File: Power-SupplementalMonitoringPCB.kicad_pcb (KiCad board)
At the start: 2 copper layers, 67.5 x 62.5 mm, 66 parts, among them J1 SWD, J2 CAN_Out, J3 CAN_Out, J4 PowerConn, J5 SuppPowerConnector, SW1 Reset, U1 STM32F413RHTx, U10 Si87xx, U2 ADM3055E, U3 CDSOT23-T24CAN, U4 RI3-1205S, U5 NCP1117-3.3_SOT223, U6 REF34-Q1, U7 OPAx192-Q1, U8 OPA388-Q1, U9 OPA388-Q1, Y1 8M

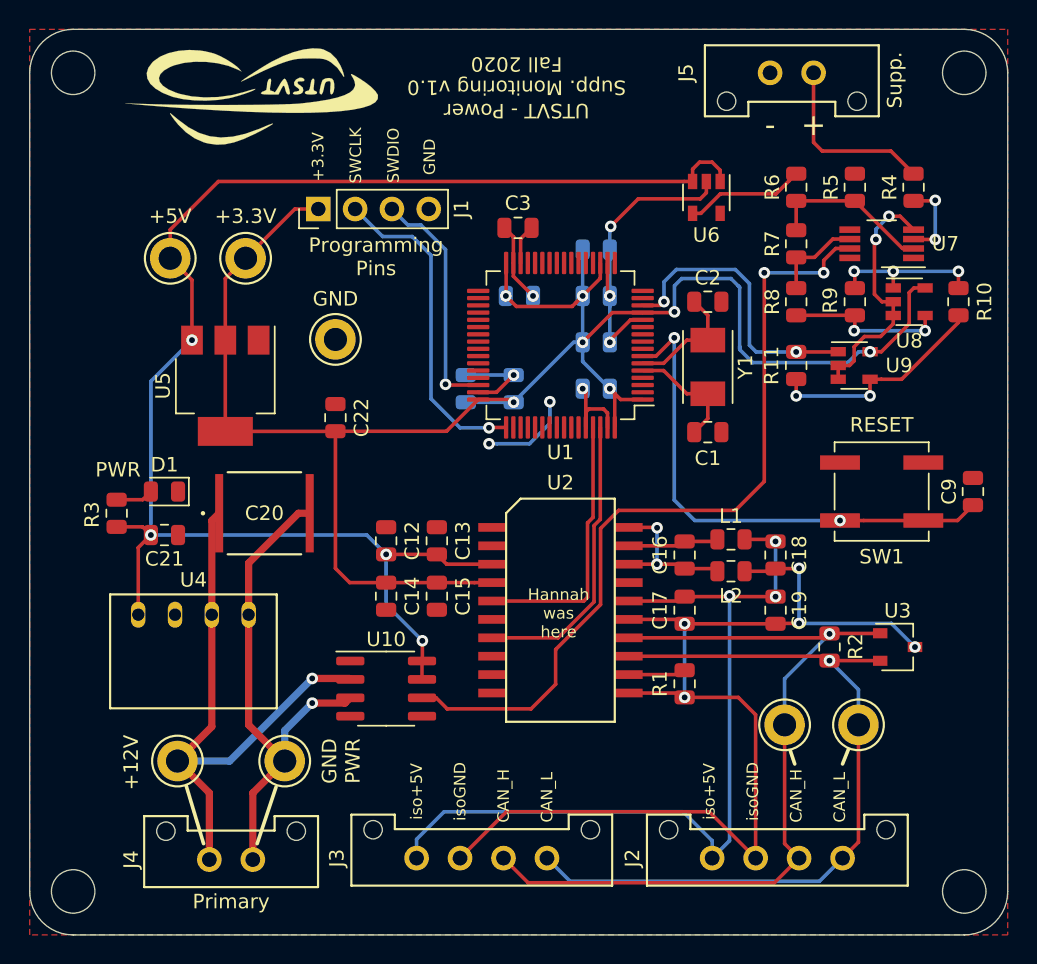
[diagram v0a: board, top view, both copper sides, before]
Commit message: Makes edits from critical design review
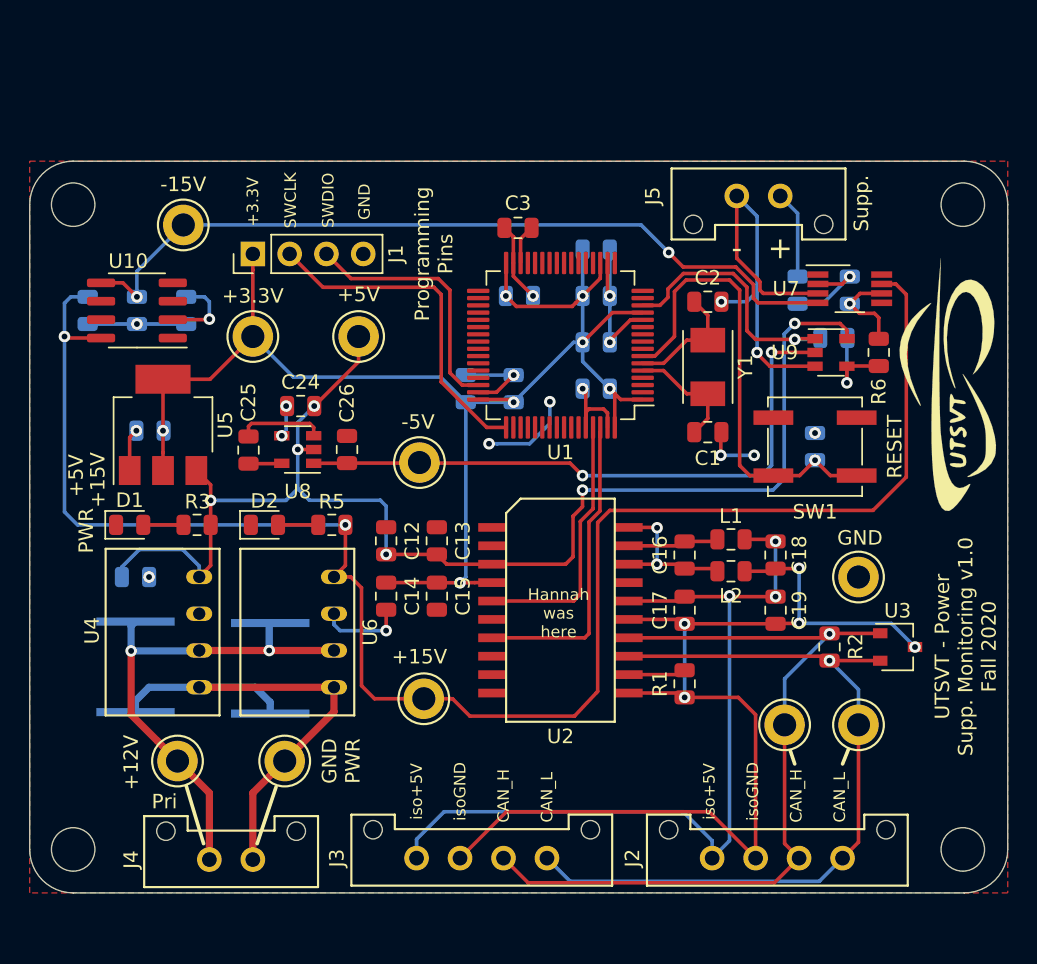
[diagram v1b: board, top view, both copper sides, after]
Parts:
- removed R10, R11, R9: 10k, Resistor_SMD:R_0805_2012Metric
- added C23: 10u, UTSVT_Passive:C_2220_5750Metric, B.Cu at (110.6, 98.5)
- added C24: 1u, Capacitor_SMD:C_0805_2012Metric, F.Cu at (112.7, 80.4)
- added C25: 1u, Capacitor_SMD:C_0805_2012Metric, F.Cu at (109.1, 83.4)
- added C26: 1u, Capacitor_SMD:C_0805_2012Metric, F.Cu at (115.9, 83.4)
- added C27: 2.2u, Capacitor_SMD:C_0805_2012Metric, B.Cu at (98.0, 73.8)
- added C28: 10u, Capacitor_SMD:C_0805_2012Metric, B.Cu at (104.8, 73.8)
- added C29: 10u, Capacitor_SMD:C_0805_2012Metric, B.Cu at (101.4, 73.8)
- added D2: PowerOn, LED_SMD:LED_0805_2012Metric, F.Cu at (110.2, 88.6)
- added TP10: -15V_TP, TestPoint:TestPoint_Keystone_5005-5009_Compact, F.Cu at (104.6, 67.9)
- added TP8: +15V_TP, TestPoint:TestPoint_Keystone_5005-5009_Compact, F.Cu at (121.2, 100.6)
- added TP9: -5V_TP, TestPoint:TestPoint_Keystone_5005-5009_Compact, F.Cu at (120.9, 84.3)
- C20, C21, C22, C9: moved to B.Cu
- R4: value 20k -> 10k; moved to B.Cu
- R5: value 20k -> 6.2k
- R7: value 20k -> 2.2k; moved to B.Cu
- R8: value 27k -> 10k; moved to B.Cu
- U10: value Si87xx -> TC7662Bx0A
- U6: value REF34-Q1 -> RI3-1215S; footprint Package_TO_SOT_SMD:SOT-23-5 -> UTSVT_ICs:RI3_DC_Converter
- U8: value OPA388-Q1 -> TPS6040x-Q1
- moved LOGO2 52.0 mm to (157.5, 79.2), turned to 90 degrees
- moved U8 43.4 mm to (112.5, 83.4), turned to 180 degrees
- moved R5 43.0 mm to (114.8, 88.6), turned to 180 degrees
- moved TP6 39.7 mm to (151.2, 92.2)
- moved U6 39.5 mm to (115.0, 96.0), turned to 90 degrees
- moved U10 31.3 mm to (101.4, 73.8), turned to 180 degrees
- moved TP5 14.1 mm to (116.7, 75.6)
- moved C20 13.8 mm to (101.3, 98.4), turned to 270 degrees
- moved C22 12.8 mm to (102.3, 82.1), turned to 180 degrees
- moved R6 12.7 mm to (152.6, 76.7)
- moved C9 11.3 mm to (148.2, 83.2)
- moved R4 10.7 mm to (147.0, 72.4)
- moved H2 9.10 mm to (158.4, 66.5)
- moved H1 9.10 mm to (97.0, 66.5)
- moved J5 8.81 mm to (145.8, 65.9)
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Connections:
- R5 pad 1: Net-(R5-Pad1) -> +15V
- R5 pad 2: GND -> Net-(D2-Pad2)
- R6 pad 1: Net-(R5-Pad1) -> Net-(R6-Pad1)
- R7 pad 1: Net-(R7-Pad1) -> Net-(R6-Pad2)
- R7 pad 2: Net-(R5-Pad1) -> Net-(R4-Pad1)
- R8 pad 1: Net-(R8-Pad1) -> /SuppOut
- R8 pad 2: Net-(R7-Pad1) -> Net-(R6-Pad1)
- U10 pad 2: +12VA -> Net-(C28-Pad1)
- U10 pad 3: GNDPWR -> GND
- U10 pad 4: Net-(U10-Pad4) -> GND
- U10 pad 5: GND -> -15V
- U10 pad 6: +12V -> Net-(U10-Pad6)
- U10 pad 7: +5V -> Net-(U10-Pad7)
- U10 pad 8: +5V -> +15V
- U6 pad 1: +5V -> GNDPWR
- U6 pad 2: GND -> +12VA
- U6 pad 3: +5V -> GND
- U6 pad 4: Net-(R6-Pad2) -> +15V
- U7 pad 2: Net-(R5-Pad1) -> Net-(R4-Pad1)
- U7 pad 3: Net-(R4-Pad1) -> GND
- U7 pad 4: GND -> -15V
- U7 pad 6: Net-(R7-Pad1) -> Net-(R6-Pad2)
- U7 pad 7: +12V -> +15V
- U8 pad 1: Net-(R10-Pad2) -> -5V
- U8 pad 2: GND -> +5V
- U8 pad 3: GND -> Net-(C25-Pad1)
- U8 pad 4: Net-(R8-Pad1) -> GND
- U8 pad 5: +3V3 -> Net-(C25-Pad2)
- U9 pad 2: GND -> -5V
- U9 pad 4: Net-(R10-Pad1) -> Net-(R6-Pad1)
- U9 pad 5: +3V3 -> +5V
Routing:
- net +15V: track 0.00 -> 118.2 mm, vias 0 -> 2
- net +12V: track 56.4 -> 0.00 mm, vias 2 -> 0
- net -15V: track 0.00 -> 55.7 mm, vias 0 -> 2
- net -5V: track 0.00 -> 43.1 mm, vias 0 -> 2
- net +3V3: track 132.0 -> 100.6 mm
- net GND: track 63.7 -> 88.4 mm, vias 10 -> 18
- net Net-(R10-Pad1): track 15.6 -> 0.00 mm, vias 2 -> 0
- net +5V: track 106.8 -> 93.5 mm, vias 4 -> 6
- net Net-(R5-Pad1): track 11.5 -> 0.00 mm
- net Net-(R8-Pad1): track 11.1 -> 0.00 mm, vias 2 -> 0
- net Net-(R10-Pad2): track 10.7 -> 0.00 mm, vias 3 -> 0
- net Net-(J5-Pad1): track 12.6 -> 6.06 mm
- net Net-(R6-Pad1): track 0.00 -> 6.47 mm, vias 0 -> 1
- net Net-(R7-Pad1): track 6.35 -> 0.00 mm
- net Net-(C25-Pad1): track 0.00 -> 5.97 mm
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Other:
- board size 67.5 x 62.5 mm -> 67.5 x 50.5 mm
- board text added: "+15V"
- board text added: "-15V"
- board text added: "-5V"
- board text added: "Pri"
- board text removed: "Primary"

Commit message: Edits opamp circuitry to just one opamp and adds keepout zone under 12V and GNDPWR
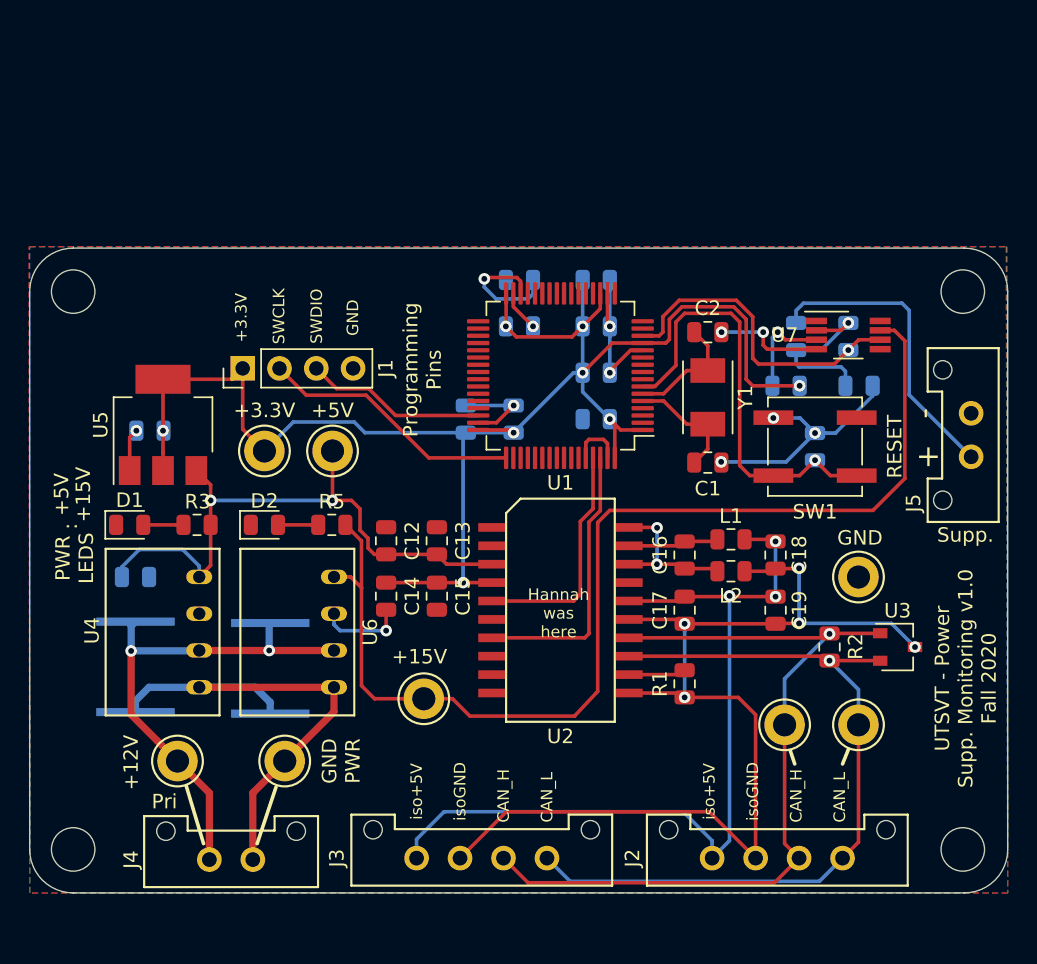
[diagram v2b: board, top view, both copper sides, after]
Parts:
- removed C24, C25, C26: 1u, Capacitor_SMD:C_0805_2012Metric
- removed C27: 2.2u, Capacitor_SMD:C_0805_2012Metric
- removed C28, C29: 10u, Capacitor_SMD:C_0805_2012Metric
- removed TP10: -15V_TP, TestPoint:TestPoint_Keystone_5005-5009_Compact
- removed TP9: -5V_TP, TestPoint:TestPoint_Keystone_5005-5009_Compact
- removed U10: TC7662Bx0A, Package_SO:SOIC-8_3.9x4.9mm_P1.27mm
- removed U8: TPS6040x-Q1, Package_TO_SOT_SMD:SOT-23-5
- removed U9: OPA388-Q1, Package_TO_SOT_SMD:SOT-23-5
- C3, LOGO2, R6: moved to B.Cu
- R8: value 10k -> 2.2k
- moved J5 22.3 mm to (159.0, 83.9), turned to 90 degrees
- moved LOGO2 19.5 mm to (157.4, 98.7), turned to 270 degrees
- moved TP5 8.10 mm to (114.9, 83.5)
- moved TP7 7.94 mm to (110.2, 83.5)
- moved J1 7.93 mm to (108.7, 77.8)
- moved H1 6.00 mm to (97.0, 72.5)
- moved H2 6.00 mm to (158.4, 72.5)
- moved R8 4.67 mm to (146.2, 79.0)
- moved LOGO1 4.40 mm to (131.1, 99.0)
- moved C3 3.60 mm to (127.8, 71.7)
- moved U7 3.20 mm to (150.5, 75.5)
- moved R4 3.20 mm to (146.9, 75.6)
- moved R7 3.20 mm to (150.5, 75.6)
- moved R6 2.67 mm to (151.2, 79.0), turned to 0 degrees
- moved C11 2.10 mm to (127.8, 74.9)
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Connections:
- R6 pad 1: Net-(R6-Pad1) -> Net-(R4-Pad1)
- R6 pad 2: Net-(R6-Pad2) -> GND
- R7 pad 1: Net-(R6-Pad2) -> /SuppOut
- R8 pad 1: /SuppOut -> Net-(R8-Pad1)
- R8 pad 2: Net-(R6-Pad1) -> +3V3
- U7 pad 3: GND -> Net-(R8-Pad1)
- U7 pad 4: -15V -> GND
- U7 pad 6: Net-(R6-Pad2) -> /SuppOut
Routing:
- net -15V: track 55.7 -> 0.00 mm, vias 2 -> 0
- net +5V: track 93.5 -> 41.8 mm, vias 6 -> 2
- net -5V: track 43.1 -> 0.00 mm, vias 2 -> 0
- net +15V: track 118.2 -> 77.3 mm, vias 2 -> 0
- net GND: track 88.4 -> 57.4 mm, vias 18 -> 11
- net Net-(J5-Pad1): track 6.06 -> 20.9 mm
- net +3V3: track 100.6 -> 112.9 mm, vias 7 -> 8
- net Net-(R8-Pad1): track 0.00 -> 6.74 mm, vias 0 -> 1
- net Net-(R6-Pad1): track 6.47 -> 0.00 mm, vias 1 -> 0
- net Net-(R6-Pad2): track 6.36 -> 0.00 mm, vias 1 -> 0
- net Net-(C3-Pad1): track 2.74 -> 8.86 mm, vias 0 -> 1
- net Net-(C25-Pad1): track 5.97 -> 0.00 mm
- net Net-(R4-Pad1): track 6.79 -> 12.4 mm
- net Net-(C28-Pad1): track 5.48 -> 0.00 mm, vias 1 -> 0
- net /SWCLK: track 23.4 -> 18.2 mm
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- added copper zone on B.Cu, net GND
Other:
- board size 67.5 x 50.5 mm -> 67.5 x 44.5 mm
- board text added: ":"
- board text added: "PWR LEDS"
- board text removed: "-15V"
- board text removed: "-5V"
- board text removed: "PWR"

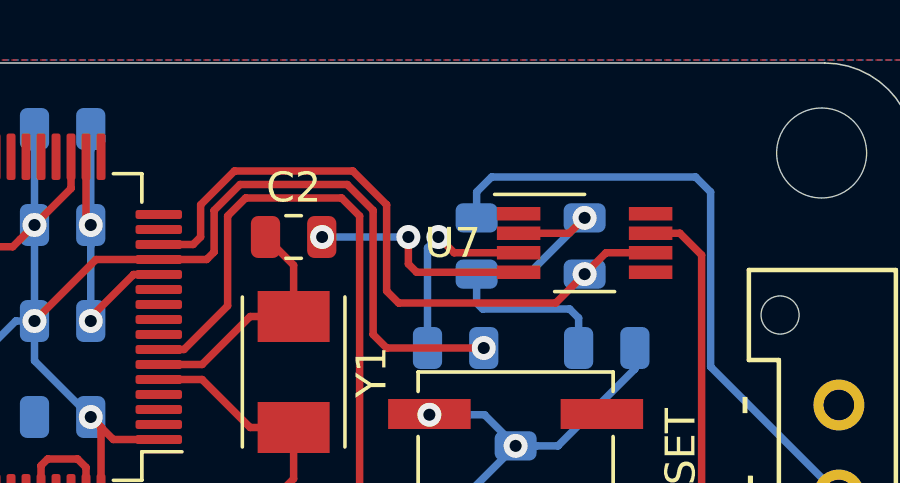
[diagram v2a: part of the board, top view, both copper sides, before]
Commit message: Fixes opamp circuitry
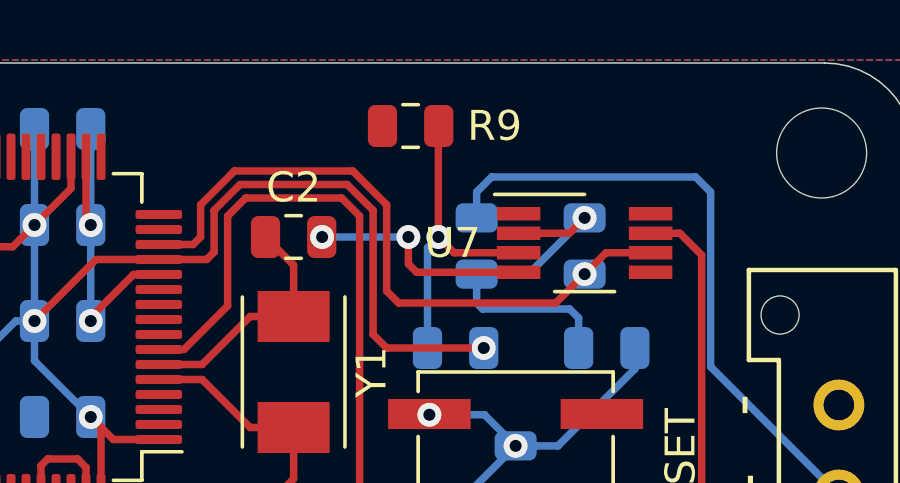
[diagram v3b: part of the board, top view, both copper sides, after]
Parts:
- added R9: 24k, Resistor_SMD:R_0805_2012Metric, F.Cu at (144.7, 71.6)
- R8: value 2.2k -> 11k
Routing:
- net Net-(R8-Pad1): track 6.74 -> 10.4 mm
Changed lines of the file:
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@@
     (thickness 1.6)
     (drawings 51)
-    (tracks 357)
+    (tracks 359)
     (zones 0)
-    (modules 63)
+    (modules 64)
     (nets 78)
   )
@@
     (add_net "Net-(U7-Pad8)")
   )
+  (module Resistor_SMD:R_0805_2012Metric (layer F.Cu)
+    (at 144.7 71.6)
+    (descr "Resistor SMD 0805 (2012 Metric), square (rectangular) end terminal, IPC_7351 nominal, (Body size source: https://docs.google.com/spreadsheets/d/1BsfQQcO9C6DZCsRaXUlFlo91Tg2WpOkGARC1WS5S8t0/edit?usp=sharing), generated with kicad-footprint-generator")
+    (tags resistor)
+    (attr smd)
+    (fp_text reference R9 (at 2.8 0) (layer F.SilkS)
+      (effects (font (size 1 1) (thickness 0.15)))
+    )
+    (fp_text value 24k (at 0 1.65) (layer F.Fab)
+      (effects (font (size 1 1) (thickness 0.15)))
+    )
+    (fp_text user %R (at 0 0) (layer F.Fab)
+      (effects (font (size 0.5 0.5) (thickness 0.08)))
+    )
+    (fp_line (start 1.68 0.95) (end -1.68 0.95) (layer F.CrtYd) (width 0.05))
+    (fp_line (start 1.68 -0.95) (end 1.68 0.95) (layer F.CrtYd) (width 0.05))
+    (fp_line (start -1.68 -0.95) (end 1.68 -0.95) (layer F.CrtYd) (width 0.05))
+    (fp_line (start -1.68 0.95) (end -1.68 -0.95) (layer F.CrtYd) (width 0.05))
+    (fp_line (start -0.258578 0.71) (end 0.258578 0.71) (layer F.SilkS) (width 0.12))
+    (fp_line (start -0.258578 -0.71) (end 0.258578 -0.71) (layer F.SilkS) (width 0.12))
+    (fp_line (start 1 0.6) (end -1 0.6) (layer F.Fab) (width 0.1))
+    (fp_line (start 1 -0.6) (end 1 0.6) (layer F.Fab) (width 0.1))
+    (fp_line (start -1 -0.6) (end 1 -0.6) (layer F.Fab) (width 0.1))
+    (fp_line (start -1 0.6) (end -1 -0.6) (layer F.Fab) (width 0.1))
+    (pad 2 smd roundrect (at 0.9375 0) (size 0.975 1.4) (layers F.Cu F.Paste F.Mask) (roundrect_rratio 0.25)
+      (net 77 "Net-(R8-Pad1)"))
+    (pad 1 smd roundrect (at -0.9375 0) (size 0.975 1.4) (layers F.Cu F.Paste F.Mask) (roundrect_rratio 0.25)
+      (net 1 GND))
+    (model ${KISYS3DMOD}/Resistor_SMD.3dshapes/R_0805_2012Metric.wrl
+      (at (xyz 0 0 0))
+      (scale (xyz 1 1 1))
+      (rotate (xyz 0 0 0))
+    )
+  )
   (module Resistor_SMD:R_0805_2012Metric (layer B.Cu)
     (at 146.2 79)
@@
     (tags resistor)
     (attr smd)
-    (fp_text reference R8 (at 0 1.65) (layer B.SilkS)
+    (fp_text reference R8 (at 0 1.7) (layer B.SilkS)
       (effects (font (size 1 1) (thickness 0.15)) (justify mirror))
     )
-    (fp_text value 2.2k (at 0 -1.65) (layer B.Fab)
+    (fp_text value 11k (at 0 -1.65) (layer B.Fab)
       (effects (font (size 1 1) (thickness 0.15)) (justify mirror))
     )
@@
   (segment (start 145.2625 75.662523) (end 145.625023 75.3) (width 0.25) (layer B.Cu) (net 77))
   (segment (start 145.2625 79) (end 145.2625 75.662523) (width 0.25) (layer B.Cu) (net 77))
+  (segment (start 145.625023 71.612477) (end 145.6375 71.6) (width 0.25) (layer F.Cu) (net 77))
+  (segment (start 145.625023 75.3) (end 145.625023 71.612477) (width 0.25) (layer F.Cu) (net 77))
   (zone (net 1) (net_name GND) (layer F.Cu) (hatch edge 0.508)
     (connect_pads yes (clearance 0.508))
